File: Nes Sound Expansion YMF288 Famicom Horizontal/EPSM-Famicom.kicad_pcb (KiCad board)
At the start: 2 copper layers, 99 x 91.7 mm, 68 parts, among them J1 CARTRIDGE_F, J2 CONSOLE_M, J3 AudioJack4_SwitchTR1, U1 74HC688, U10 74HC132, U11 74HC257, U12 74HC257, U13 LM358, U14 74LVC1G373, U15 74HC257, U2 74HC139, U3 74HC174, U4 74HC174, U5 74HC688, U6 74HC688, U7 74HC132, U8 YMF288, U9 BU9480F, X1 SG-8002CA

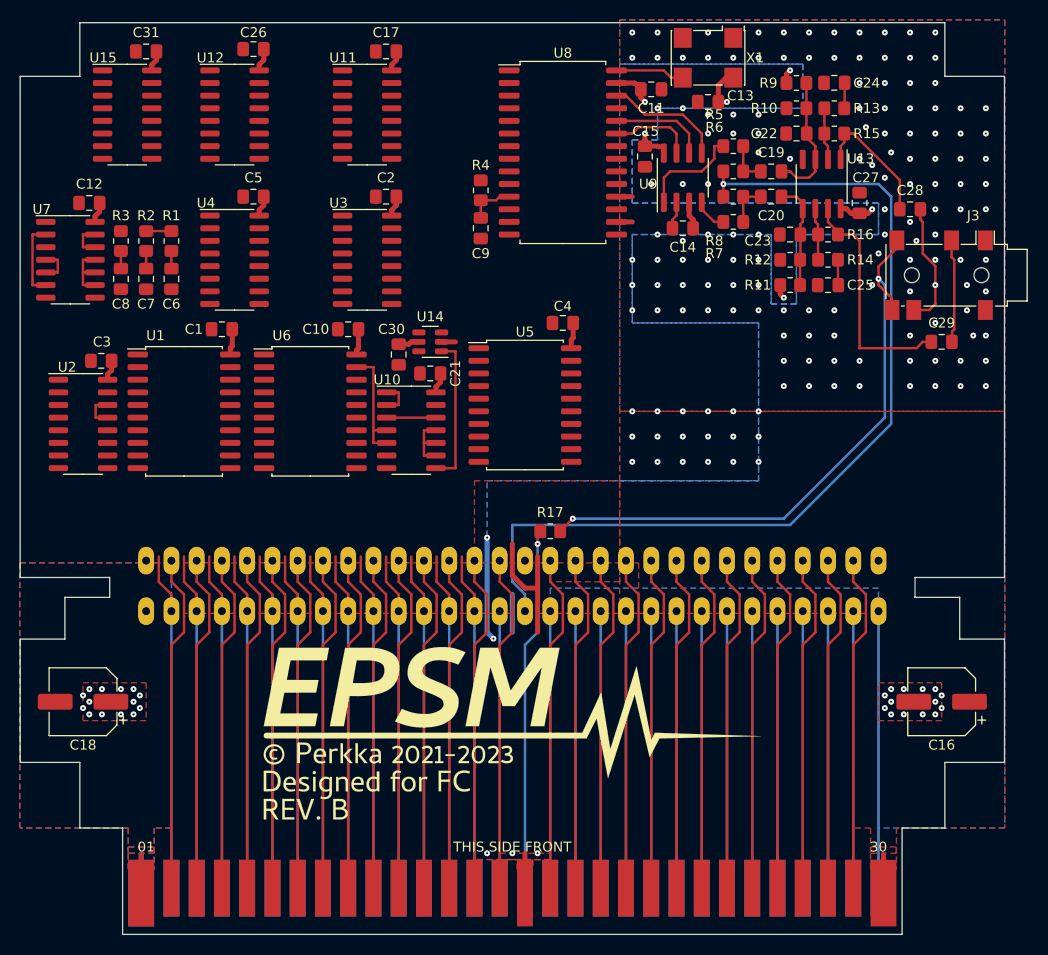
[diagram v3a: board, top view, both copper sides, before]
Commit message: Improved routing
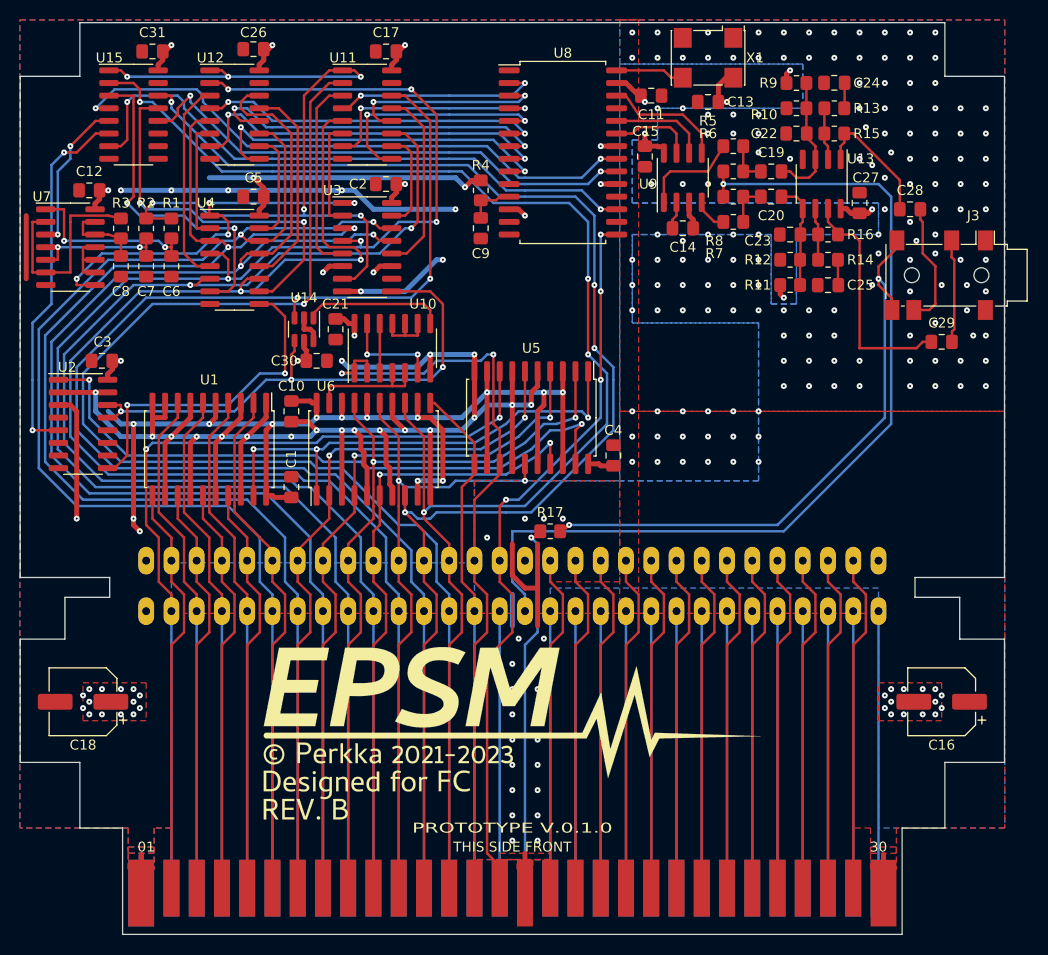
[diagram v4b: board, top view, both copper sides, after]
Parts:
- moved C1 17.3 mm to (104.8, 92.7), turned to -90 degrees
- moved C4 14.3 mm to (137.2, 89.5), turned to -90 degrees
- moved U14 12.8 mm to (106.0, 76.8), turned to -90 degrees
- moved C21 10.5 mm to (109.2, 76.8), turned to 90 degrees
- moved C10 10.0 mm to (104.8, 85.1), turned to 90 degrees
- moved U10 8.47 mm to (114.9, 78.7), turned to 90 degrees
- moved C30 8.28 mm to (107.3, 80.0), turned to 180 degrees
- moved U6 7.41 mm to (113.0, 88.9), turned to 90 degrees
- moved U1 4.58 mm to (96.5, 88.9), turned to -90 degrees
- moved U5 1.42 mm to (128.9, 85.7), turned to -90 degrees
- moved C6 1.27 mm to (92.7, 70.5)
- moved C7 1.27 mm to (90.2, 70.5)
- moved C8 1.27 mm to (87.6, 70.5)
- moved R1 1.27 mm to (92.7, 66.7)
- moved R2 1.27 mm to (90.2, 66.7)
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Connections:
- U1 pad 11: /CPU_A7 -> /CPU_A11
- U1 pad 13: /CPU_A8 -> /CPU_A10
- U1 pad 15: /CPU_A14 -> /CPU_A9
- U1 pad 16: VCC -> GND
- U1 pad 17: /CPU_A9 -> /CPU_A8
- U1 pad 2: /CPU_A13 -> /CPU_A7
- U1 pad 4: /CPU_A10 -> /CPU_A14
- U1 pad 5: GND -> VCC
- U1 pad 6: /CPU_A12 -> /CPU_A13
- U1 pad 8: /CPU_A11 -> /CPU_A12
- U15 pad 14: /EPSM_A0 -> /CPU_A1
- U15 pad 2: /EPSM_A1 -> /CPU_A0
- U5 pad 11: /CPU_R~{W} -> /~{ROMSEL}
- U5 pad 12: GND -> VCC
- U5 pad 13: /~{ROMSEL} -> /CPU_R~{W}
- U5 pad 14: VCC -> GND
- U5 pad 2: /M2 -> /CPU_A4
- U5 pad 4: /CPU_A6 -> /CPU_A5
- U5 pad 6: /CPU_A5 -> /CPU_A6
- U5 pad 8: /CPU_A4 -> /M2
- U6 pad 15: /CPU_A1 -> /CPU_A2
- U6 pad 17: /CPU_A2 -> /CPU_A4
- U6 pad 2: /CPU_A3 -> /CPU_A6
- U6 pad 4: /CPU_A4 -> /CPU_A5
- U6 pad 5: VCC -> GND
- U6 pad 6: /CPU_A5 -> /CPU_A3
- U6 pad 8: /CPU_A6 -> /CPU_A1
- U6 pad 9: GND -> VCC
- U7 pad 12: Net-(U7-Pad12) -> Net-(C8-Pad1)
- U7 pad 13: Net-(U7-Pad12) -> Net-(C8-Pad1)
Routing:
- net GND: track 43.3 -> 248.7 mm, vias 152 -> 195
- net VCC: track 53.6 -> 225.7 mm, vias 38 -> 68
- net /CPU_D4: track 33.9 -> 162.3 mm, vias 0 -> 5
- net /CPU_A0: track 34.0 -> 149.6 mm, vias 0 -> 4
- net /CPU_D1: track 33.9 -> 141.7 mm, vias 0 -> 2
- net /CPU_D5: track 33.9 -> 141.4 mm, vias 0 -> 2
- net /CPU_A1: track 34.0 -> 138.9 mm, vias 0 -> 4
- net /CPU_D2: track 33.9 -> 134.2 mm, vias 0 -> 2
- net /CPU_D3: track 33.9 -> 132.5 mm, vias 0 -> 2
- net /CPU_D7: track 33.9 -> 131.7 mm, vias 0 -> 2
- net /CPU_D0: track 33.9 -> 130.5 mm, vias 0 -> 1
- net /CPU_D6: track 33.9 -> 129.9 mm, vias 0 -> 2
- net /$4016_EN: track 2.54 -> 81.6 mm, vias 0 -> 6
- net /$401x_~{CE}: track 0.00 -> 64.3 mm, vias 0 -> 2
- net /YM_CS: track 0.00 -> 60.5 mm, vias 0 -> 2
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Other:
- board text added: "PROTOTYPE V.0.1.0"

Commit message: Fix swapped connections
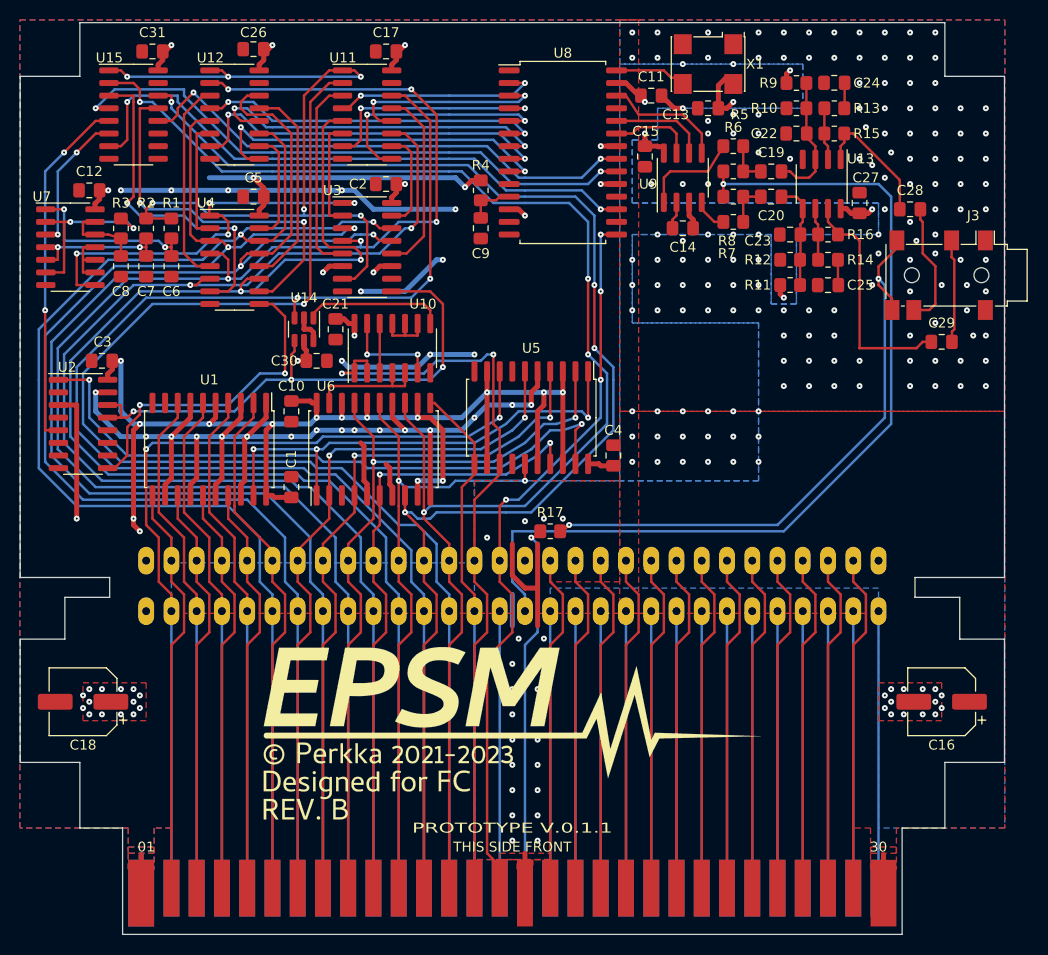
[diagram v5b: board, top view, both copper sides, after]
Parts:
- moved C13 0.63 mm to (146.7, 54.6)
- moved X1 0.63 mm to (146.7, 50.2)
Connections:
- U15 pad 12: /YM_A0 -> /YM_A1
- U15 pad 4: /YM_A1 -> /YM_A0
- U15 pad 5: /BUF_CS -> /~{CS}
- U15 pad 6: /~{CS} -> /BUF_CS
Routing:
- net GND: track 248.7 -> 199.9 mm, vias 195 -> 194
- net /YM_A1: track 59.4 -> 52.0 mm
- net /YM_A0: track 52.1 -> 59.4 mm
- net VCC: track 225.7 -> 231.4 mm
- net Net-(R3-Pad1): track 21.1 -> 17.6 mm, vias 0 -> 2
- net /FF_RESET: track 40.0 -> 41.5 mm
- net /~{CS}: track 37.2 -> 35.9 mm
- net /BUF_CS: track 15.5 -> 14.3 mm
- net /~{OUT_1}: track 33.6 -> 32.9 mm
- net /OUT_1: track 53.9 -> 54.5 mm
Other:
- board text added: "PROTOTYPE V.0.1.1"
- board text removed: "PROTOTYPE V.0.1.0"
